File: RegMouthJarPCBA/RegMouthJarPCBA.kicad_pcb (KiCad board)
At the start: 2 copper layers, 70 x 70 mm, 14 parts, among them CON1 BARREL_JACK, J1 4P4C, J2 4P4C, K1 CONN_3, P2 CONN_4, P3 CONN_4

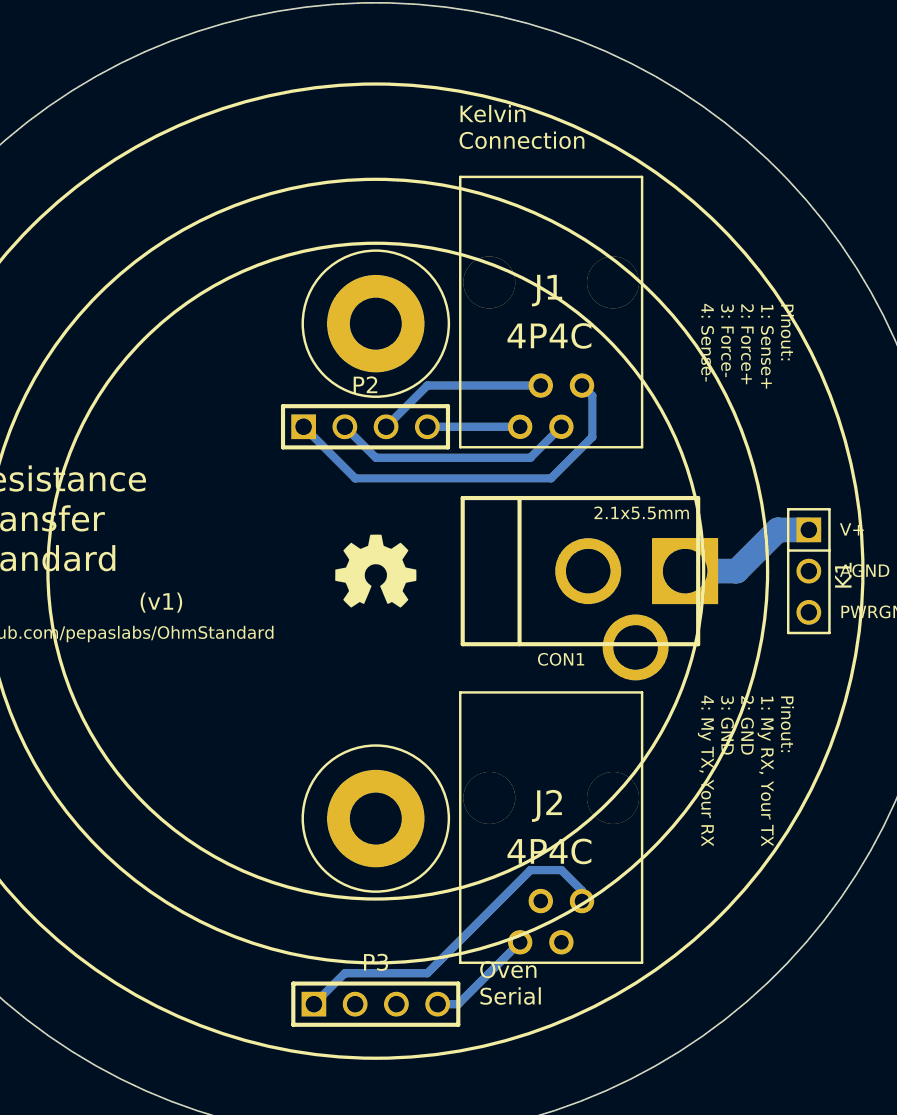
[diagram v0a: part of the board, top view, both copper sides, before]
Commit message: adding temperature test point
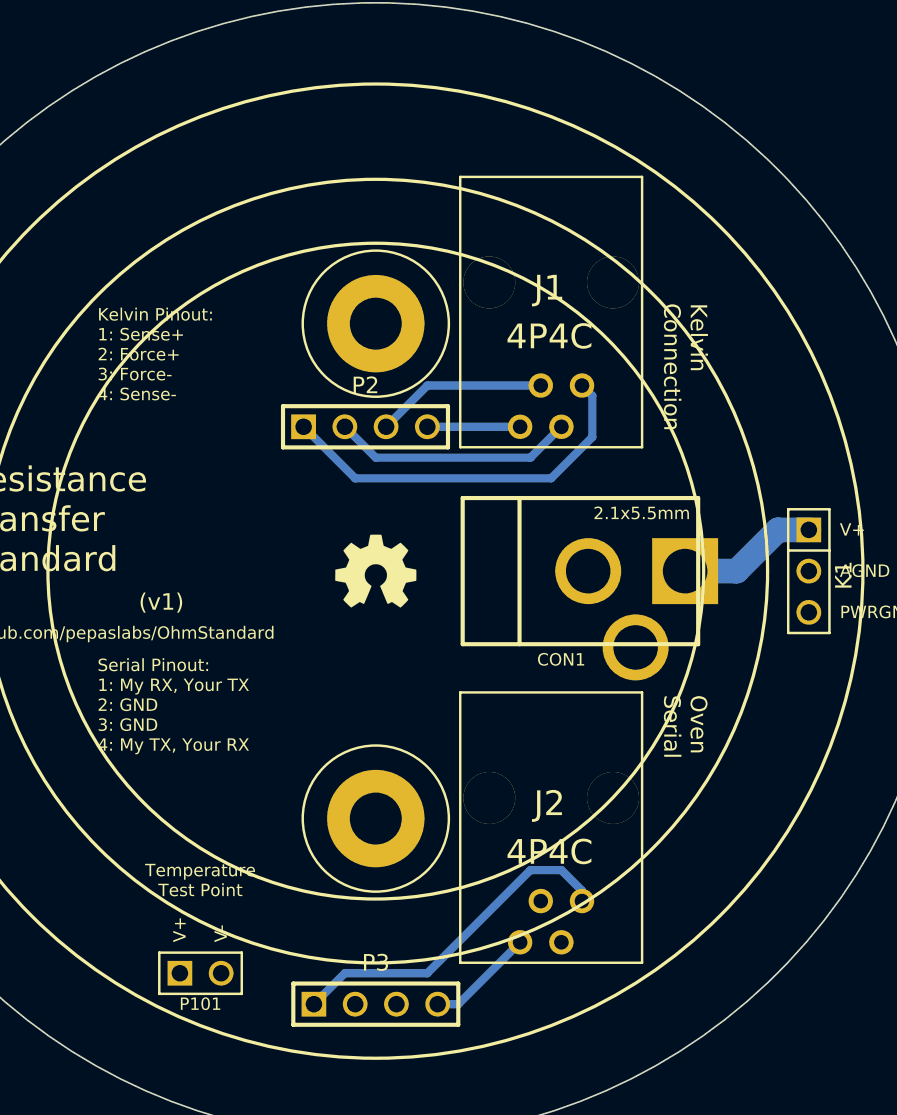
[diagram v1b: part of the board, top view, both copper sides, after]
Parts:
- added P101: CONN_2, PIN_ARRAY_2X1, F.Cu at (-10.8, 24.8)
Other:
- board text added: "Kelvin Pinout: 1: Sense+ 2: Force+ 3: Force- 4: Sense-"
- board text added: "Serial Pinout: 1: My RX, Your TX 2: GND 3: GND 4: My TX, Your RX"
- board text added: "Temperature Test Point"
- board text added: "V-"
- board text removed: "Pinout: 1: My RX, Your TX 2: GND 3: GND 4: My TX, Your RX"
- board text removed: "Pinout: 1: Sense+ 2: Force+ 3: Force- 4: Sense-"

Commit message: tweaking board layout.
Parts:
- removed the G*** at (0.00, 0.00)
- removed U*** (x2): VAL**, DIP8
- removed U***: VAL**, TO-92_U
- removed Val** (x2): U***, TO-220_V_069B
- added G***: OSHW-logo_silkscreen-front_4mm, OSHW-logo_silkscreen-front_4mm, F.Cu at (-16.5, 0.00)
- moved P4 28.9 mm to (-25.7, 0.00), turned to 270 degrees
- moved J1 21.9 mm to (-8.89, -7.62)
- moved J2 21.9 mm to (-8.89, 16.5)
- moved P1 20.4 mm to (17.8, 18.4), turned to 45 degrees
- moved CON1 7.62 mm to (11.4, 0.00), turned to 180 degrees
- moved P2 1.91 mm to (1.27, -8.89)
- moved P3 1.02 mm to (0.00, 25.7)
- renumbered K1 to P1, P101 to P4
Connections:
- J2 pad 2: GND -> N-000008
- J2 pad 3: GND -> N-000009
- P3 pad 2: GND -> N-000008
- P3 pad 3: GND -> N-000009
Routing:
- net N-000009: track 0.00 -> 19.7 mm
- net N-0000010: track 6.66 -> 25.9 mm
- net N-0000012: track 23.6 -> 6.88 mm
- net N-000008: track 0.00 -> 16.3 mm
- net N-000001: track 5.72 -> 22.1 mm
- net N-000007: track 21.1 -> 11.2 mm
- net N-000004: track 8.67 -> 0.00 mm
- net N-0000014: track 10.6 -> 16.8 mm
- net N-0000013: track 14.9 -> 12.9 mm
- added copper zone on B.Cu, net N-000004
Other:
- board size 70 x 70 mm -> 68.1 x 68.1 mm

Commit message: finalizing v1 board design and creating gerbers.
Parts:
- moved H1 278.5 mm to (221.0, 154.3)
- moved J1 278.5 mm to (212.1, 161.9)
- moved J2 278.5 mm to (212.1, 186.1)
- moved P1 278.5 mm to (238.8, 188.0)
- moved P2 278.5 mm to (222.2, 160.7)
- moved P3 278.5 mm to (221.0, 195.2)
- moved CON1 278.5 mm to (232.4, 169.5)
- moved G*** 278.5 mm to (204.5, 169.5)
- moved H2 278.5 mm to (221.0, 184.8)
- moved P4 278.5 mm to (195.3, 169.5)
